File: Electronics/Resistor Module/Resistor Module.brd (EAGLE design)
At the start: 50 x 50 mm, 121 parts, among them U1 74HC595D, U2 74HC595D, U3 74HC595D, U4 74HC595D, U5 25AA010A

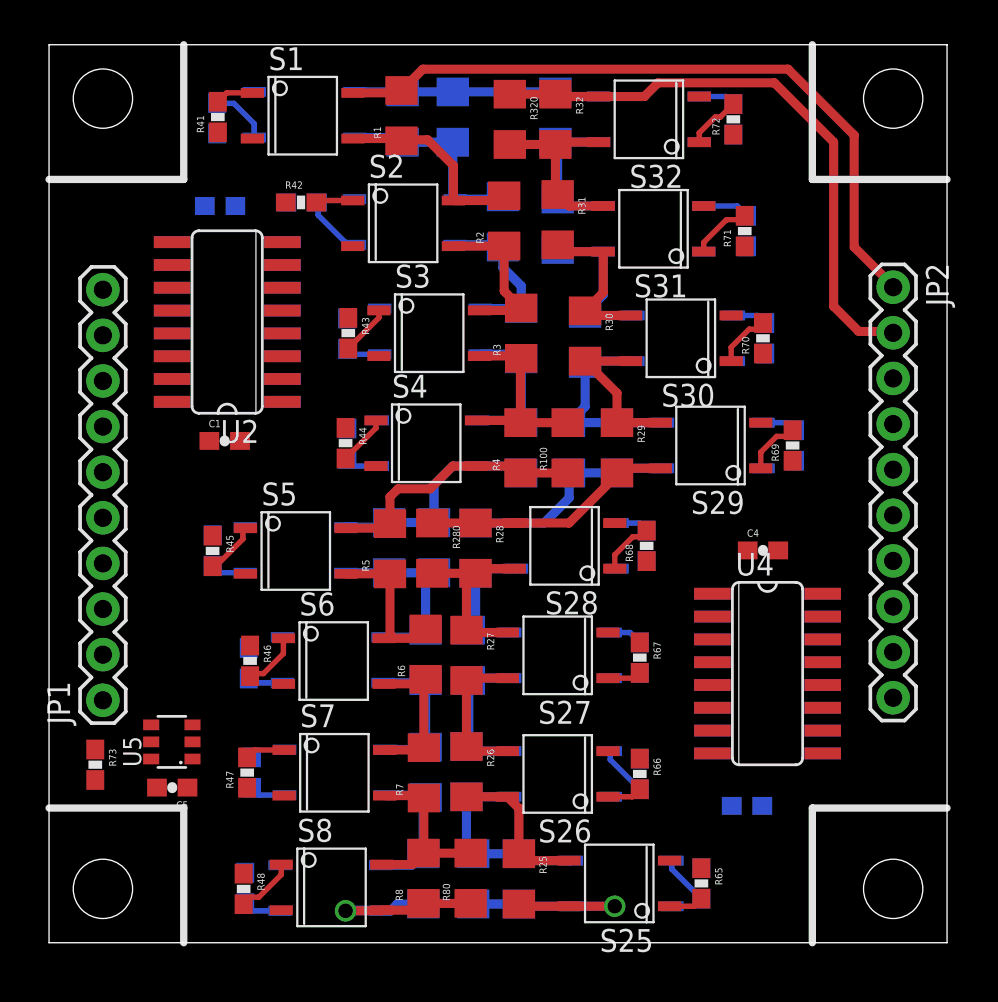
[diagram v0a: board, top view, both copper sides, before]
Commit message: Tied control nets for serial shifters to connectors and each other. Only need to route relay signals now.
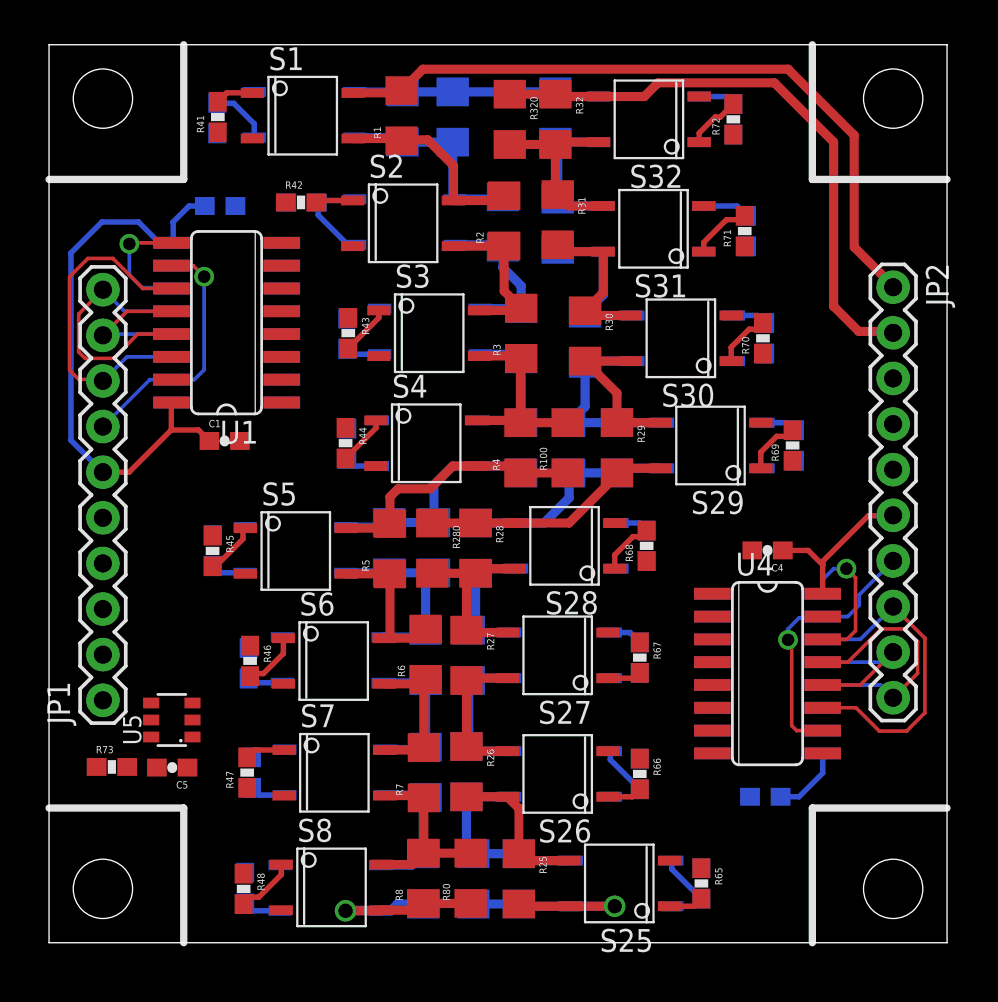
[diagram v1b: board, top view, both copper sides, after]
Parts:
- moved U5 1.22 mm to (6.84, 12.4)
- moved C3 1.14 mm to (39.9, 8.13)
- moved C5 1.12 mm to (6.86, 9.75)
- moved R73 0.93 mm to (3.50, 9.79), turned to 0 degrees
- moved C4 0.25 mm to (40.0, 21.8), turned to 180 degrees
- moved U1 0.06 mm to (9.88, 34.5), flipped to the top, turned to 90 degrees
- flipped U2 to the bottom, turned to 270 degrees
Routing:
- net 5V: track 0.00 -> 31.8 mm
- net SERIAL_CLK: track 0.00 -> 18.5 mm
- net SERIAL_CLK_2: track 0.00 -> 18.0 mm
- net SERIAL_MR_L_2: track 0.00 -> 15.1 mm, vias 0 -> 1
- net SERIAL_OE_L_2: track 0.00 -> 14.2 mm
- net SERIAL_OE_L: track 0.00 -> 14.2 mm
- net SERIAL_MR_L: track 0.00 -> 14.2 mm, vias 0 -> 1
- net 5V_2: track 0.00 -> 13.3 mm
- net SERIAL_LATCH_2: track 0.00 -> 8.83 mm
- net SERIAL_LATCH: track 0.00 -> 8.21 mm
- net SERIAL_PASS2: track 0.00 -> 8.05 mm, vias 0 -> 1
- net SERIAL_PASS: track 0.00 -> 6.75 mm, vias 0 -> 1

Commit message: Finished routing. Was more convenient for routing to use inverted byte order for the serial passing.
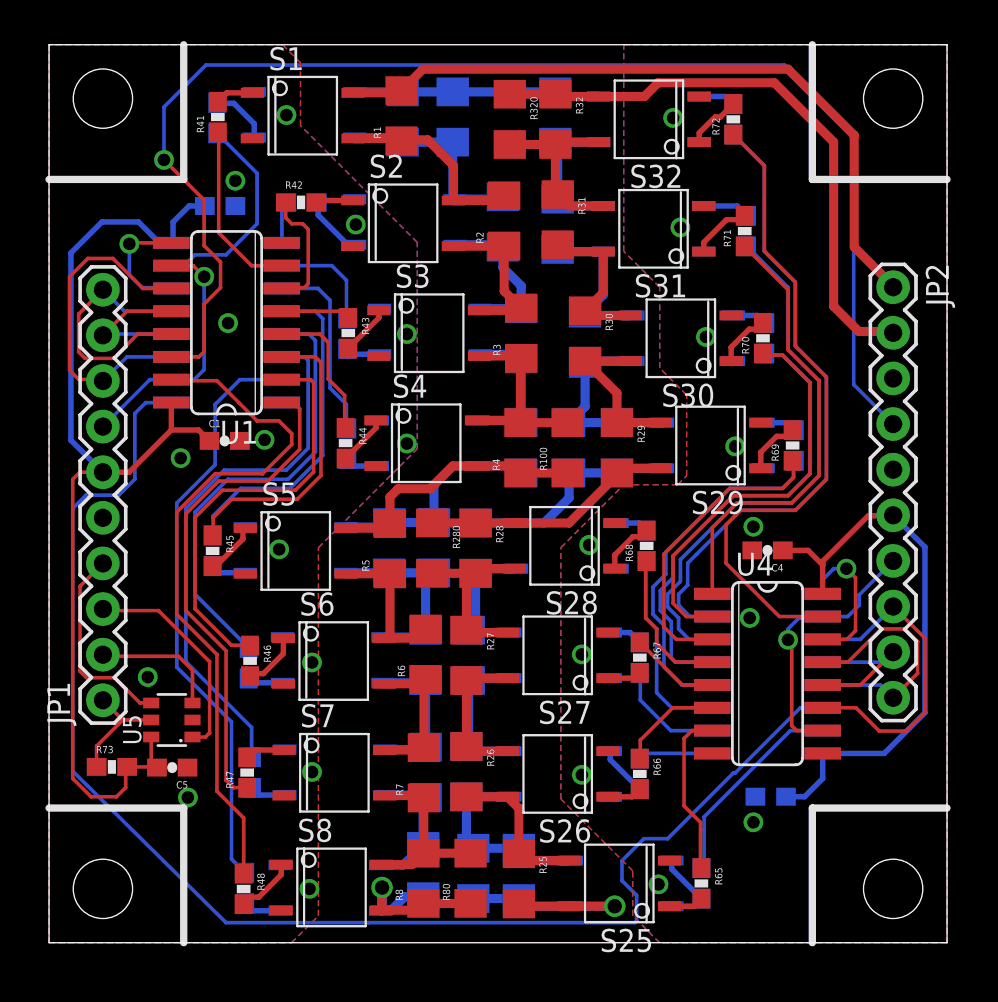
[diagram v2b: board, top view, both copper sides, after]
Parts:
- moved R9 0.41 mm to (20.8, 3.96)
- moved C3 0.30 mm to (40.2, 8.13)
- moved R24 0.30 mm to (26.2, 3.86)
- moved R240 0.30 mm to (23.6, 3.86)
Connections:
- removed net N$61: R49.1, U2.15
- removed net N$62: R57.1, U3.15
- removed net N$64: R65.1, U4.15
- new net N$40: R67.1, U4.5
- new net N$43: R66.1, U4.6
- new net N$9: R46.1, U1.2
- net GND: no longer S17.P2, S18.P2, S19.P2, S20.P2, S21.P2, S22.P2, S23.P2, S24.P2, S25.P2, S26.P2, S27.P2, S28.P2, S29.P2, S30.P2, S31.P2, S32.P2
- net GND_2: now also S17.P2, S18.P2, S19.P2, S20.P2, S21.P2, S22.P2, S23.P2, S24.P2, S25.P2, S26.P2, S27.P2, S28.P2, S29.P2, S30.P2, S31.P2, S32.P2
- net N$1: now also U1.15; no longer U1.7
- net N$12: now also R45.1, U1.3; no longer R46.1, U1.5
- net N$13: now also R44.1; no longer R45.1
- net N$14: now also R43.1, U1.5; no longer R44.1, U1.3
- net N$16: now also R42.1, U1.6; no longer R43.1, U1.2
- net N$17: now also R41.1, U1.7; no longer R42.1, U1.1
- net N$18: now also R56.1, U2.15; no longer R50.1, U2.1
- net N$19: now also R55.1, U2.1; no longer R51.1, U2.2
- net N$2: now also U1.1; no longer U1.6
- net N$20: now also R54.1, U2.2; no longer R52.1, U2.3
- net N$21: now also U2.3; no longer U2.4
- net N$22: now also R52.1, U2.4; no longer R54.1, U2.5
- net N$23: now also R51.1, U2.5; no longer R55.1, U2.6
- net N$24: now also R50.1, U2.6; no longer R56.1, U2.7
- net N$26: now also R49.1, U2.7; no longer R64.1, U3.7
- net N$27: now also R64.1, U3.15; no longer R63.1, U3.6
- net N$28: now also R63.1, U3.1; no longer R62.1, U3.5
- net N$29: now also R62.1, U3.2; no longer R61.1, U3.4
- net N$30: now also R61.1; no longer R60.1
- net N$31: now also R60.1, U3.4; no longer R59.1, U3.2
- net N$32: now also R59.1, U3.5; no longer R58.1, U3.1
- net N$33: now also R58.1, U3.6; no longer R66.1, U4.1
- net N$34: now also R57.1, U3.7; no longer R67.1, U4.2
- net N$35: now also R72.1, U4.15; no longer R68.1, U4.3
- net N$36: now also R71.1, U4.1; no longer R69.1, U4.4
- net N$37: now also U4.2; no longer U4.5
- net N$38: now also R69.1, U4.3; no longer R71.1, U4.6
- net N$39: now also R68.1, U4.4; no longer R72.1, U4.7
- net N$57: now also R65.1, U4.7; no longer R41.1, U1.15
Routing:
- net SERIAL_PASS1: track 0.00 -> 78.0 mm
- net SERIAL_IN: track 0.00 -> 75.3 mm, vias 0 -> 1
- net N$1: track 0.00 -> 38.2 mm
- net N$35: track 0.00 -> 36.7 mm
- net N$34: track 0.00 -> 35.7 mm
- net N$26: track 0.00 -> 32.8 mm
- net N$33: track 0.00 -> 30.6 mm
- net N$24: track 0.00 -> 30.0 mm
- net N$2: track 0.00 -> 28.3 mm
- net 5V: track 31.8 -> 60.0 mm
- net N$32: track 0.00 -> 26.4 mm
- net N$36: track 0.00 -> 25.3 mm
- net N$23: track 0.00 -> 25.1 mm
- net N$9: track 0.00 -> 23.5 mm
- net N$37: track 0.00 -> 23.0 mm
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- added copper zone on layer 1, net GND
- added copper zone on layer 16, net GND
- added copper zone on layer 1, net GND_2
- added copper zone on layer 16, net GND_2

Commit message: Finished routing and silk cleanup. Ready for final review and release.
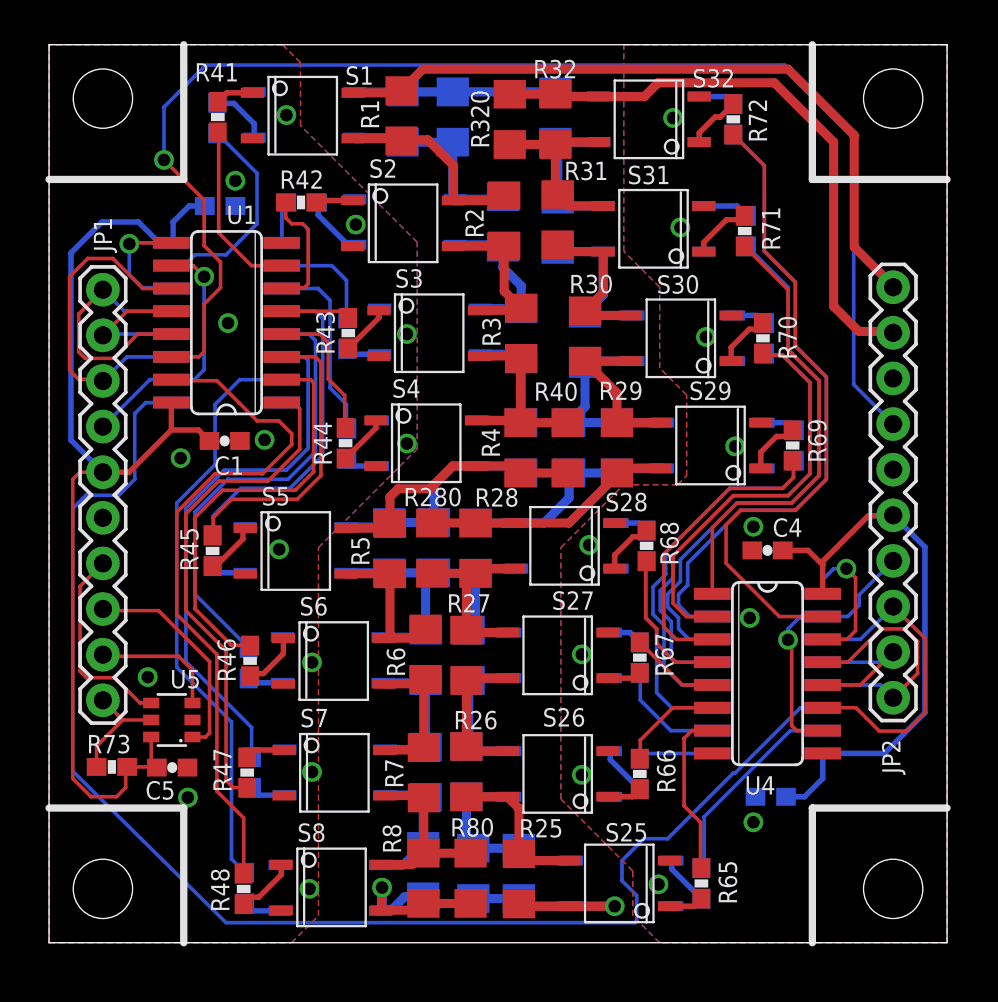
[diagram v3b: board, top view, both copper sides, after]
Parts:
- renumbered R100 to R40

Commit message: Added silk documentation and part numbers. Fixed a few minor placement issues and silk errors. Updated gerbers for manufacture and completed review. Will submit for DFM and order boards today hopefully.
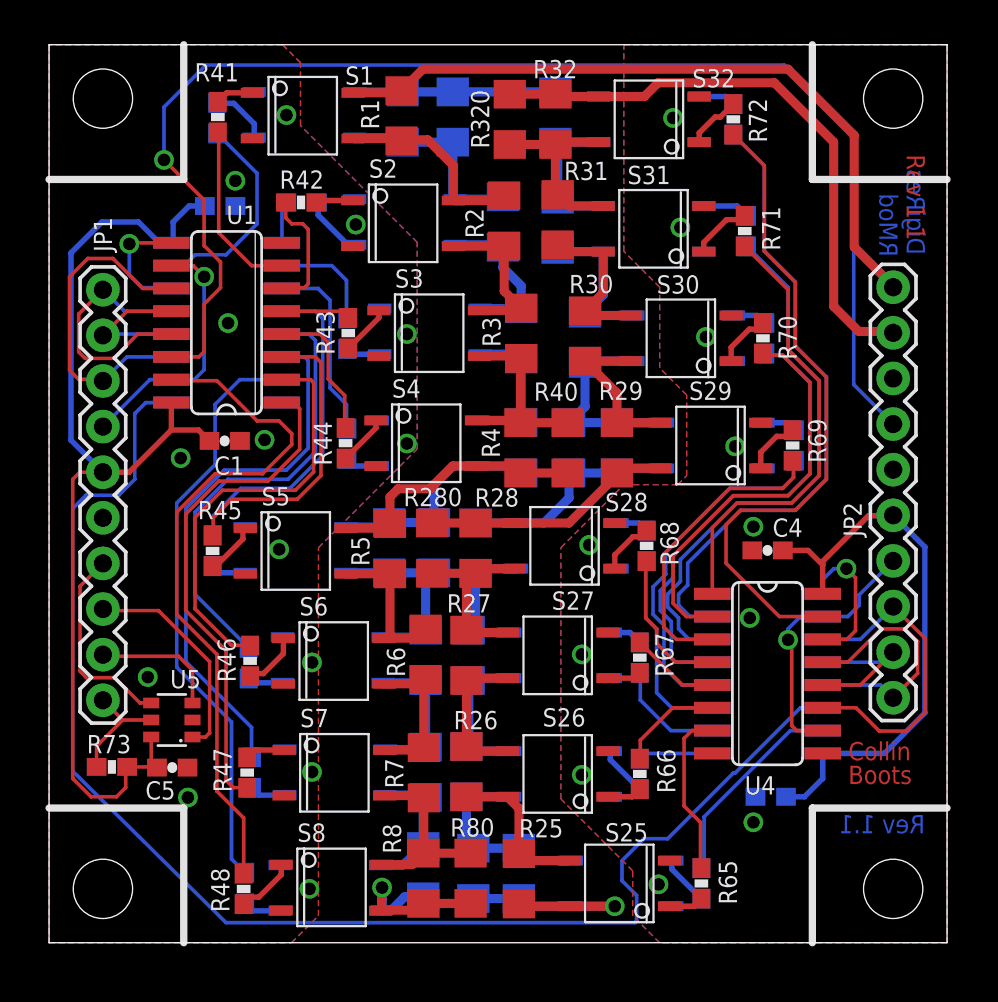
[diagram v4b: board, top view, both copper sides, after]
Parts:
- JP1, JP2: value M10PASSTHROUGH -> M10-PPPC101LFBN-RC; device Resistor Module Library:U4CON_18688_10 -> Resistor Module Library:PPPC101LFBN-RC
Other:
- board text added: "Boots"
- board text added: "Collin"
- board text added: "Collin Boots"
- board text added: "DigiRes"
- board text added: "DigiRes-RMod"
- board text added: "RMod"
- board text added: "Rev 1.1"
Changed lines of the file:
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@@
 <wire x1="50" y1="42.5" x2="42.5" y2="42.5" width="0.4064" layer="21"/>
 <wire x1="42.5" y1="42.5" x2="42.5" y2="50" width="0.4064" layer="21"/>
+<text x="5.7912" y="16.0528" size="1.016" layer="51" font="vector" rot="R90">DigiRes-RMod</text>
+<text x="7.0104" y="16.0528" size="1.016" layer="51" font="vector" rot="R90">Collin Boots</text>
+<text x="43.2816" y="38.2016" size="1.016" layer="52" font="vector" rot="MR90">DigiRes-RMod</text>
+<text x="44.8056" y="38.2016" size="1.016" layer="52" font="vector" rot="MR90">Rev 1.1</text>
+<text x="8.2296" y="16.0528" size="1.016" layer="51" font="vector" rot="R90">Rev 1.1</text>
+<text x="47.752" y="38.3032" size="1.016" layer="16" font="vector" ratio="20" rot="MR90">DigiRes</text>
+<text x="46.228" y="38.2016" size="1.016" layer="16" font="vector" ratio="20" rot="MR90">RMod</text>
+<text x="41.656" y="38.2016" size="1.016" layer="26" font="vector" rot="MR90">Collin Boots</text>
+<text x="48.768" y="6.096" size="1.016" layer="16" font="vector" ratio="20" rot="MR0">Rev 1.1</text>
+<text x="47.752" y="43.8912" size="1.016" layer="1" font="vector" ratio="20" rot="SR270">Rev 1.1</text>
+<text x="44.5008" y="10.16" size="1.016" layer="1" font="vector" ratio="20" rot="SR0">Collin</text>
+<text x="44.5008" y="8.8392" size="1.016" layer="1" font="vector" ratio="20" rot="SR0">Boots</text>
 </plain>
 <attributes>
@@
 </element>
 <element name="R45" library="Resistor Module Library" package="0603-RES" value="2k" x="9.106" y="21.815" smashed="yes" rot="R270">
-<attribute name="NAME" x="8.3184" y="20.6792" size="1.016" layer="25" font="vector" rot="R90"/>
+<attribute name="NAME" x="8.284" y="23.584" size="1.016" layer="25" font="vector"/>
 <attribute name="VALUE" x="7.963" y="22.831" size="0.4064" layer="27" font="vector" rot="R270"/>
 </element>
@@
 <attribute name="VALUE" x="2.4822" y="8.6456" size="0.4064" layer="27" font="vector"/>
 </element>
-<element name="JP1" library="Resistor Module Library" package="U4CON_18688_10" value="M10PASSTHROUGH" x="3" y="13.5" smashed="yes" rot="R90">
+<element name="JP1" library="Resistor Module Library" package="PPPC101LFBN-RC" value="M10-PPPC101LFBN-RC" x="3" y="13.5" smashed="yes" rot="R90">
 <attribute name="NAME" x="3.508" y="38.4682" size="1.016" layer="25" font="vector" ratio="10" rot="R90"/>
 <attribute name="VALUE" x="6.175" y="12.23" size="1.27" layer="27" rot="R90"/>
 </element>
-<element name="JP2" library="Resistor Module Library" package="U4CON_18688_10" value="M10PASSTHROUGH" x="47" y="36.5" smashed="yes" rot="R270">
-<attribute name="NAME" x="46.3904" y="11.3286" size="1.016" layer="25" font="vector" ratio="10" rot="R270"/>
+<element name="JP2" library="Resistor Module Library" package="PPPC101LFBN-RC" value="M10-PPPC101LFBN-RC" x="47" y="36.5" smashed="yes" rot="R270">
+<attribute name="NAME" x="45.2528" y="22.6058" size="1.016" layer="25" font="vector" ratio="10" rot="R90"/>
 <attribute name="VALUE" x="43.825" y="37.77" size="1.27" layer="27" rot="R270"/>
 </element>
